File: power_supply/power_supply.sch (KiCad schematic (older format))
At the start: 45 parts, among them J1 Conn_01x04_Male, J2 Conn_01x03_Male, J3 Conn_01x03_Male, J4 Conn_01x03_Male, U1 LM7815_TO220, U2 LM7915_TO220, U3 LM7805_TO220

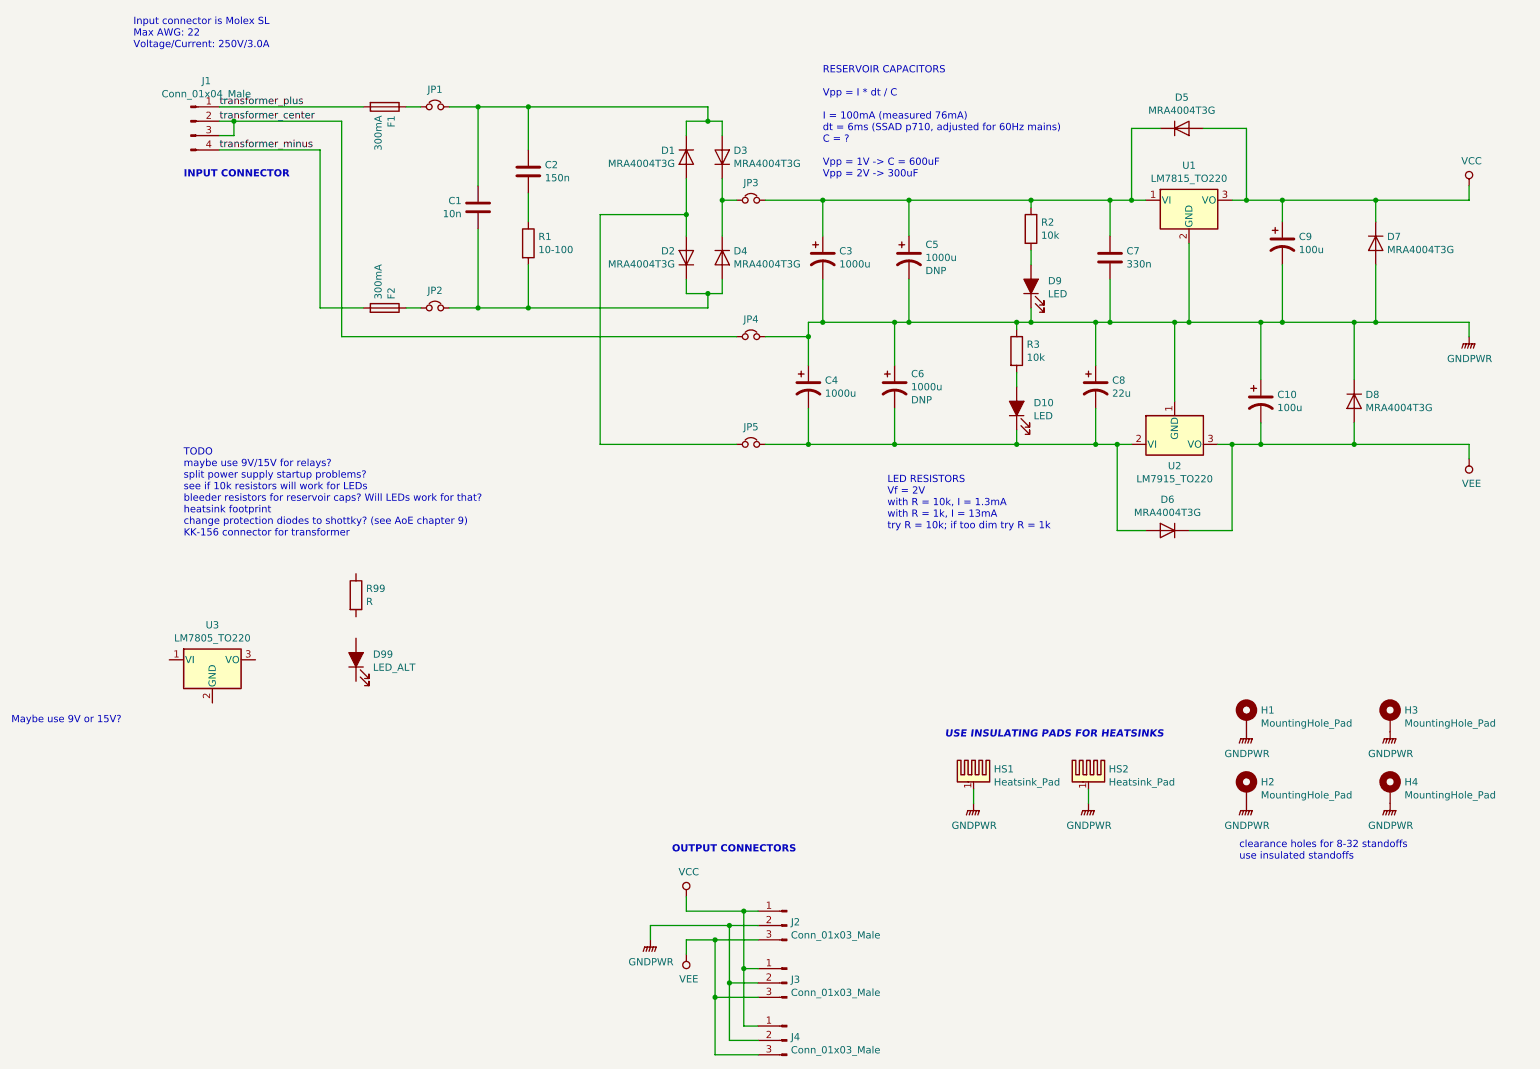
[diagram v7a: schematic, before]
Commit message: add aux (relay/front panel power supply) to schematics/pcb. Also cleanup DRC violations in schematic
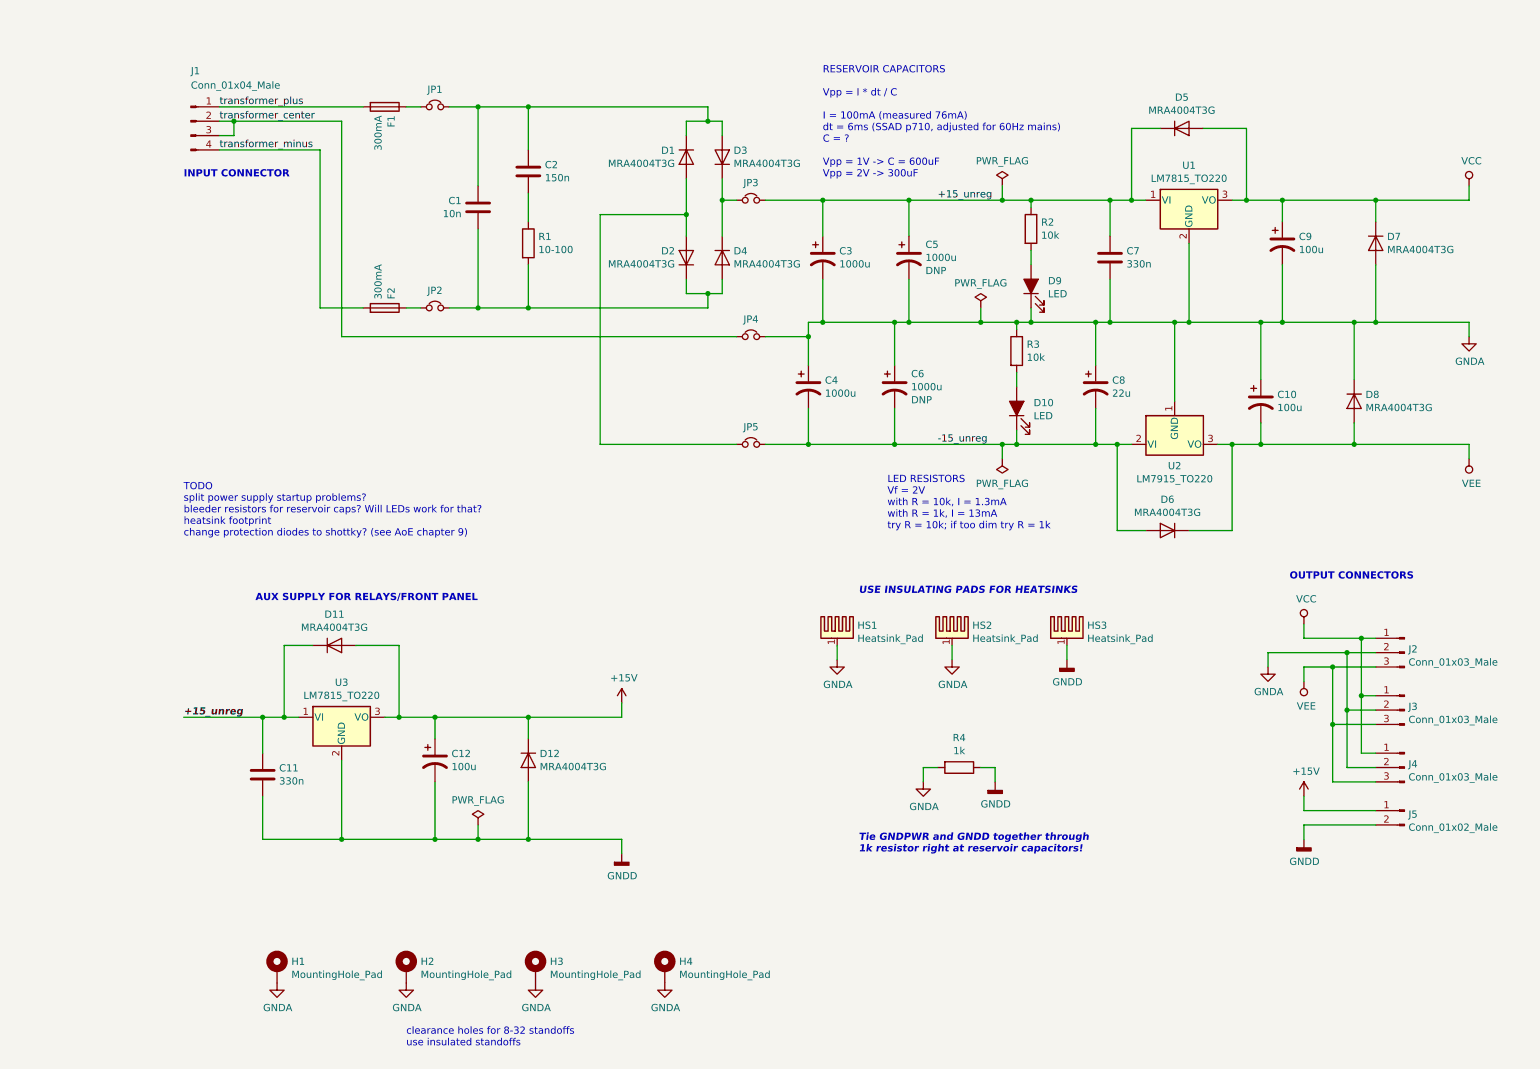
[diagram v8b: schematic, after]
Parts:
- removed D99: LED_ALT, LED_SMD:LED_0603_1608Metric_Pad1.05x0.95mm_HandSolder, symbol Device:LED_ALT
- removed R99: R, Resistor_SMD:R_0603_1608Metric_Pad1.05x0.95mm_HandSolder, symbol Device:R
- removed U3: LM7805_TO220, Package_TO_SOT_THT:TO-220-3_Vertical, symbol Regulator_Linear:LM7805_TO220
- added C11: 330n, Capacitor_SMD:C_0805_2012Metric_Pad1.15x1.40mm_HandSolder, symbol Device:C
- added C12: 100u, Capacitor_THT:CP_Radial_D6.3mm_P2.50mm, symbol Device:CP1
- added D11, D12: MRA4004T3G, Diode_SMD:D_SMA, symbol Diode:MRA4004T3G
- added HS3: Heatsink_Pad, Heatsink:Heatsink_35x26mm_1xFixation3mm_Fischer-SK486-35, symbol Mechanical:Heatsink_Pad
- added J5: Conn_01x02_Male, Connector_Molex_SL:Molex_SL_A-70543-0001_1x02_P2.54mm_Vertical, symbol Connector:Conn_01x02_Male
- added R4: 1k, Resistor_SMD:R_0603_1608Metric_Pad1.05x0.95mm_HandSolder, symbol Device:R
- added U3: LM7815_TO220, Package_TO_SOT_THT:TO-220-3_Vertical, symbol Regulator_Linear:LM7815_TO220
- HS1, HS2: footprint (none) -> Heatsink:Heatsink_35x26mm_1xFixation3mm_Fischer-SK486-35
- J1: footprint Connector_Molex_SL:Molex_SL_A-70543-0003_1x04_P2.54mm_Vertical -> Connector_Molex_KK-396:Molex_KK-396_A-41791-0004_1x04_P3.96mm_Vertical
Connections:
- net +15_unreg: now reaches C3.1, C5.1, C7.1, D5.1 (K), JP3.2, R2.1, U1.1 (VI)
- net +15_unreg: now also C11.1, D11.1 (K), U3.1 (VI)
- net -15_unreg: now reaches C4.2, C6.2, C8.2, D10.1 (K), D6.2 (A), JP5.2, U2.2 (VI)
- net GNDPWR renamed GNDA
- net GNDA: now also R4.2
- new net +15V: C12.1, D11.2 (A), D12.1 (K), J5.1 (Pin_1), U3.3 (VO)
- new net GNDD: C11.2, C12.2, D12.2 (A), HS3.1, J5.2 (Pin_2), R4.1, U3.2 (GND)
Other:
- note added: "AUX SUPPLY FOR RELAYS/FRONT PANEL"
- note added: "TODO\nsplit power supply startup problems?\nbleeder resistors for reservoir caps? Will LEDs work for that?\nheatsink footprint\nchange protection diodes to shottky? (see AoE chapter 9)"
- note added: "Tie GNDPWR and GNDD together through\n1k resistor right at reservoir capacitors!"
- note removed: "Input connector is Molex SL\nMax AWG: 22\nVoltage/Current: 250V/3.0A"
- note removed: "Maybe use 9V or 15V?"
- note removed: "TODO\nmaybe use 9V/15V for relays?\nsplit power supply startup problems?\nsee if 10k resistors will work for LEDs\nbleeder resistors for reservoir caps? Will LEDs work for that?\nheatsink footprint\nchange protection diodes to shottky? (see AoE chapter 9)\nKK-156 connector for transformer"
- moved on the sheet: H1, H2, H3, H4, HS1, HS2, J2, J3, J4
